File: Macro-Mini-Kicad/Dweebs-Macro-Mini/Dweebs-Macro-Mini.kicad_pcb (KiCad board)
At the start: 2 copper layers, 133.3 x 111.1 mm, 57 parts, among them U1 ProMicro

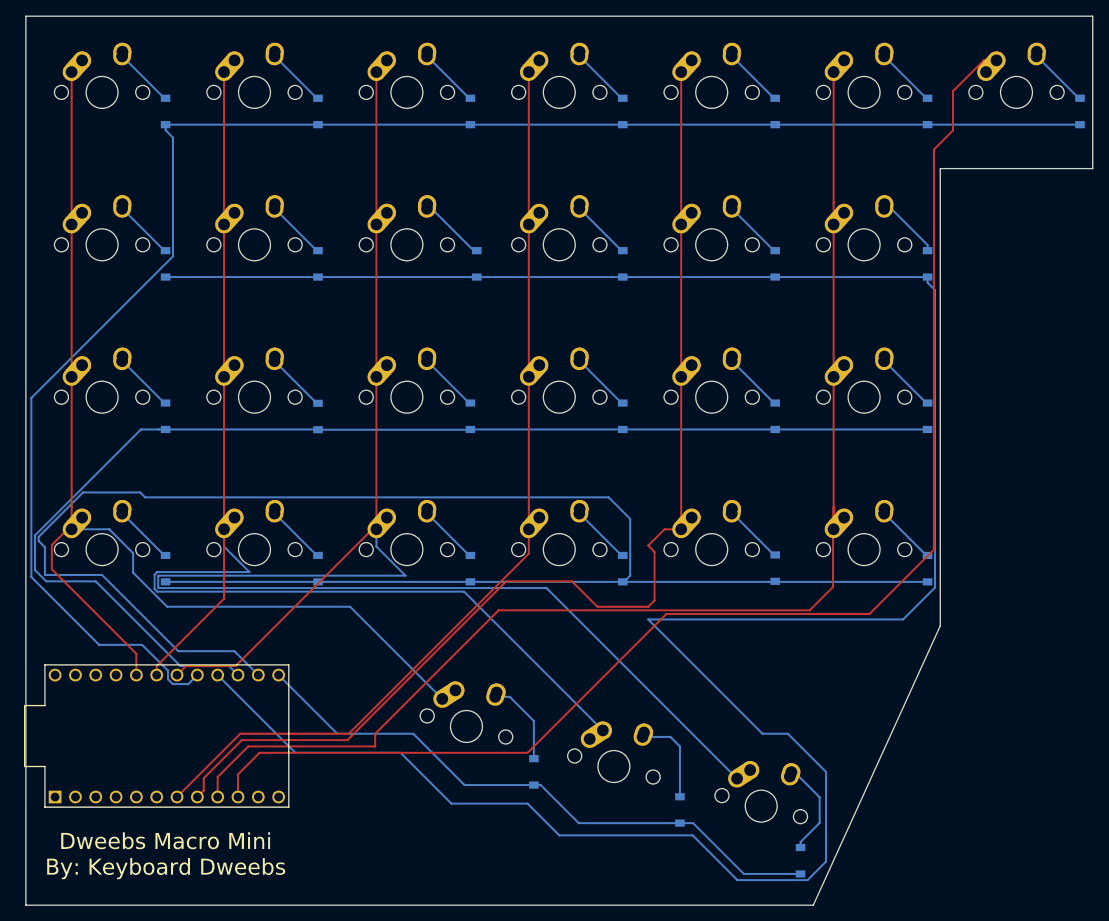
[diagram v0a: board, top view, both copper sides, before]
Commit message: updated cut to match vector
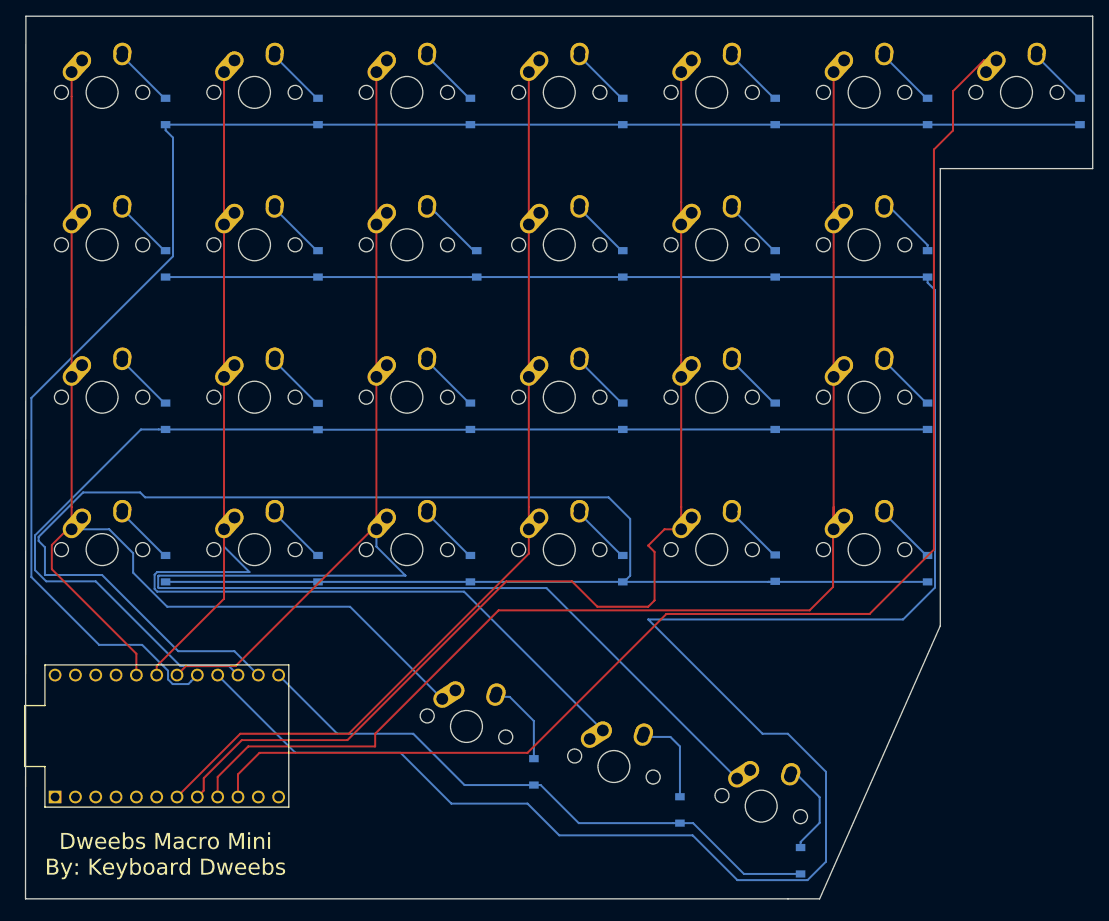
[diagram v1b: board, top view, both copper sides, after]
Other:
- board size 133.3 x 111.1 mm -> 133.4 x 110.3 mm
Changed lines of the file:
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@@
   (general
     (thickness 1.6)
-    (drawings 10)
+    (drawings 11)
     (tracks 277)
     (zones 0)
@@
     )
   )
+  (gr_line (start 73.772884 150.018562) (end 73.81875 39.6875) (layer Edge.Cuts) (width 0.05))
+  (gr_line (start 173.0375 150.01875) (end 188.11875 115.8875) (layer Edge.Cuts) (width 0.05))
+  (gr_line (start 169.06875 150.01875) (end 173.0375 150.01875) (layer Edge.Cuts) (width 0.05))
+  (gr_line (start 169.06875 150.01875) (end 73.772884 150.018562) (layer Edge.Cuts) (width 0.05))
   (gr_text "Dweebs Macro Mini\nBy: Keyboard Dweebs" (at 91.28125 144.4625) (layer F.SilkS)
     (effects (font (size 2 2) (thickness 0.15)))
@@
   (gr_line (start 207.16875 39.6875) (end 207.16875 58.7375) (layer Edge.Cuts) (width 0.05))
   (gr_line (start 73.81875 39.6875) (end 207.16875 39.6875) (layer Edge.Cuts) (width 0.05))
-  (gr_line (start 73.81875 150.8125) (end 73.81875 39.6875) (layer Edge.Cuts) (width 0.05))
-  (gr_line (start 172.24375 150.8125) (end 73.81875 150.8125) (layer Edge.Cuts) (width 0.05))
-  (gr_line (start 188.11875 115.8875) (end 172.24375 150.8125) (layer Edge.Cuts) (width 0.05))
   (segment (start 85.9 44.7125) (end 85.84375 44.7125) (width 0.25) (layer B.Cu) (net 1))
   (segment (start 91.13125 49.94375) (end 85.9 44.7125) (width 0.25) (layer B.Cu) (net 1))
